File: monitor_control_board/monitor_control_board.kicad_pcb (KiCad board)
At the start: 2 copper layers, 50 x 65.1 mm, 10 parts, among them J1 Conn_01x08_Male, J2 Conn_01x08_Male, J3 Conn_01x08_Male, SW1 SW_Push, SW2 SW_Push, SW3 SW_Push, SW4 SW_Push, SW5 SW_Push, SW6 SW_Push

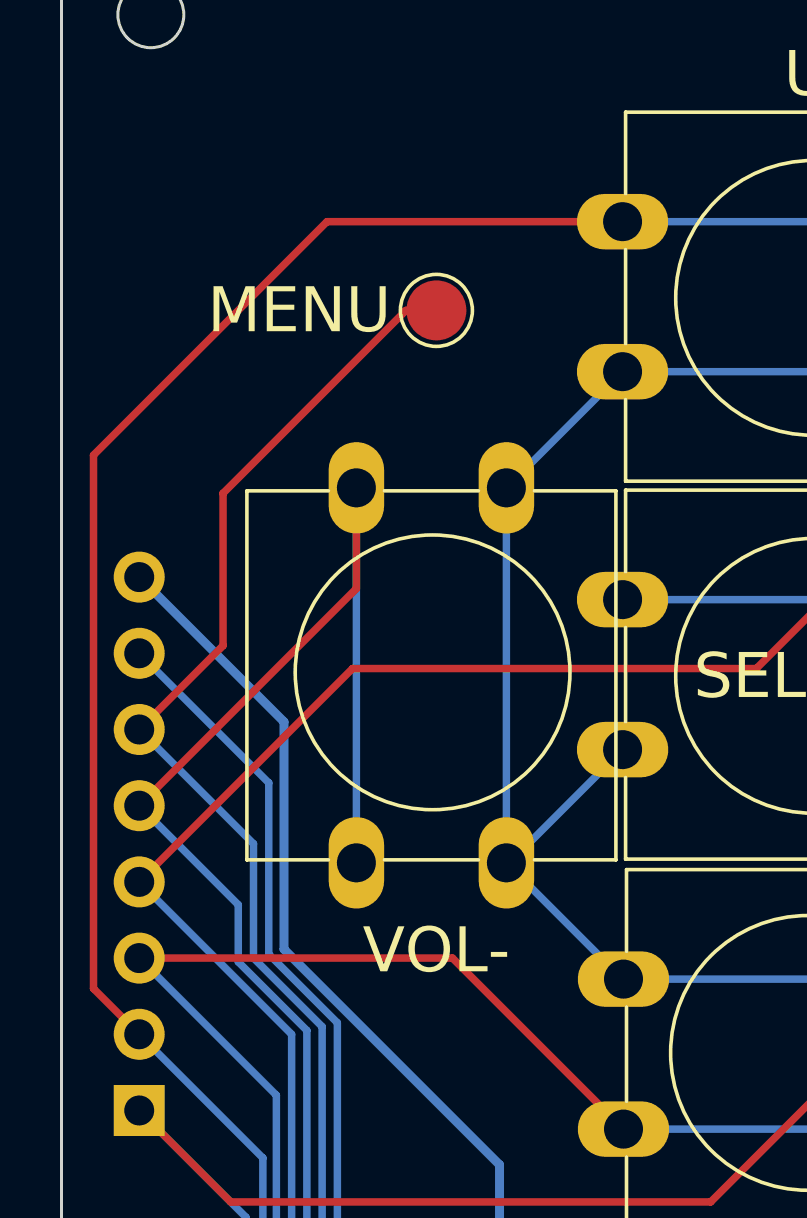
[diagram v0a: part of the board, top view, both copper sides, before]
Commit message: monitor control board에 GND TP 추가
Signed-off-by: Ju, Gyeong-min <jcmh74@gmail.com>
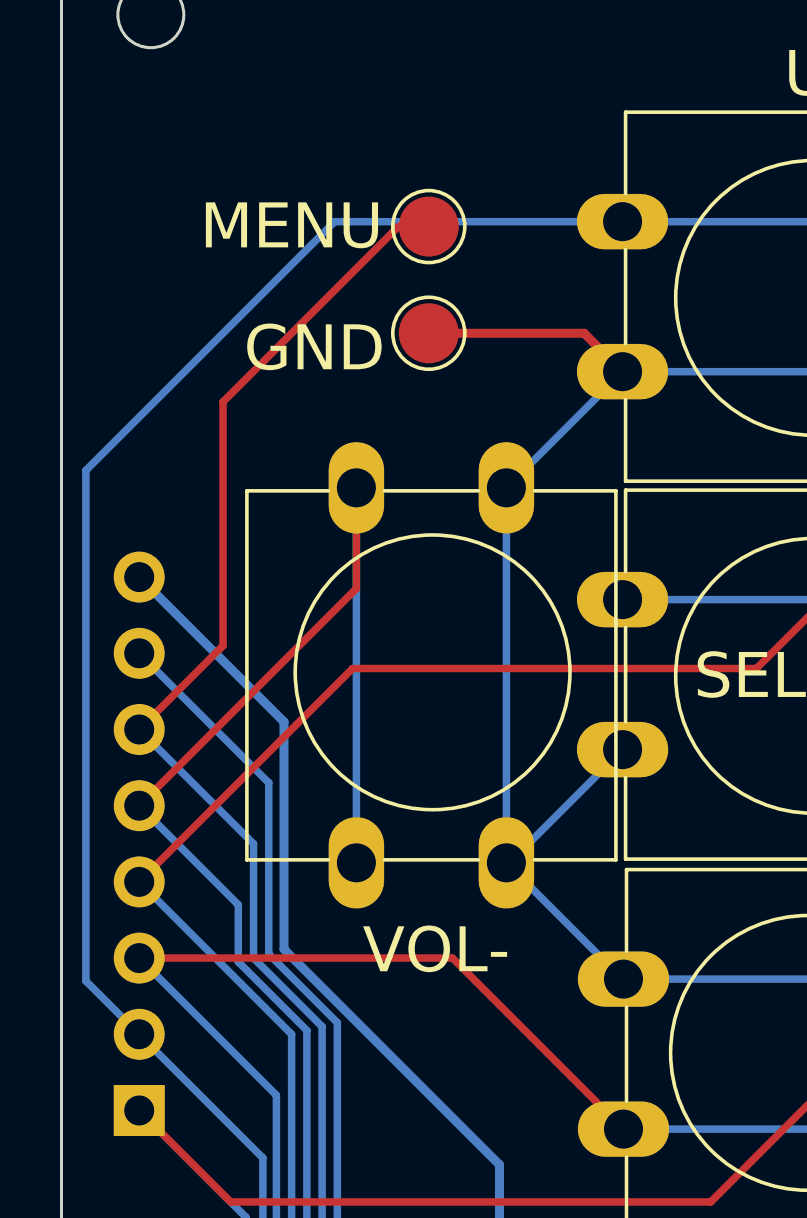
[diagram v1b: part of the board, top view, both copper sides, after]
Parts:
- added TP2: TestPoint, TestPoint:TestPoint_Pad_D2.0mm, F.Cu at (141.0, 71.4)
- moved TP1 2.81 mm to (141.0, 67.8)
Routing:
- net GND: track 198.2 -> 205.2 mm
- net /MENU: track 67.3 -> 70.0 mm
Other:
- board text added: "GND"
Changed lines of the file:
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@@
   )
   (footprint "TestPoint:TestPoint_Pad_D2.0mm" (layer "F.Cu")
-    (at 141.224 70.612)
+    (at 140.97 67.818)
     (descr "SMD pad as test Point, diameter 2.0mm")
     (tags "test point SMD pad")
@@
     )
   )
+  (footprint "TestPoint:TestPoint_Pad_D2.0mm" (layer "F.Cu")
+    (at 140.97 71.374)
+    (descr "SMD pad as test Point, diameter 2.0mm")
+    (tags "test point SMD pad")
+    (property "Sheetfile" "monitor_control_board.kicad_sch")
+    (property "Sheetname" "")
+    (attr exclude_from_pos_files)
+    (fp_text reference "TP2" (at 0 -1.998) (layer "F.SilkS") hide
+      (effects (font (size 1 1) (thickness 0.15)))
+    )
+    (fp_text value "TestPoint" (at 0 2.05) (layer "F.Fab")
+      (effects (font (size 1 1) (thickness 0.15)))
+    )
+    (fp_text user "${REFERENCE}" (at 0 -2) (layer "F.Fab")
+      (effects (font (size 1 1) (thickness 0.15)))
+    )
+    (fp_circle (center 0 0) (end 0 1.2) (layer "F.SilkS") (width 0.12) (fill none))
+    (fp_circle (center 0 0) (end 1.5 0) (layer "F.CrtYd") (width 0.05) (fill none))
+    (pad "1" smd circle (at 0 0) (size 2 2) (layers "F.Cu" "F.Mask")
+      (net 7 "GND") (pinfunction "1") (pintype "passive"))
+  )
   (footprint "Button_Switch_THT:SW_PUSH-12mm" (layer "F.Cu")
     (at 159.9608 97.9024 180)
@@
     (effects (font (size 1.5 1.5) (thickness 0.3)))
   )
-  (gr_text "MENU" (at 136.652 70.612) (layer "F.SilkS")
+  (gr_text "MENU" (at 136.398 67.818) (layer "F.SilkS")
     (effects (font (size 1.5 1.5) (thickness 0.3)))
   )
@@
     (effects (font (size 1.5 1.5) (thickness 0.3)))
   )
+  (gr_text "GND" (at 137.16 71.882) (layer "F.SilkS")
+    (effects (font (size 1.5 1.5) (thickness 0.3)))
+  )
   (gr_text "VOL+" (at 166.37 91.948) (layer "F.SilkS")
     (effects (font (size 1.5 1.5) (thickness 0.3)))
@@
   (segment (start 162.052 117.602) (end 159.766 119.888) (width 0.3) (layer "B.Cu") (net 1))
   (segment (start 134.874 100.838) (end 131.318 97.282) (width 0.25) (layer "B.Cu") (net 1))
-  (segment (start 131.318 94.742) (end 129.794 93.218) (width 0.25) (layer "F.Cu") (net 2))
-  (segment (start 129.794 93.218) (end 129.794 75.438) (width 0.25) (layer "F.Cu") (net 2))
-  (segment (start 129.794 75.438) (end 137.5772 67.6548) (width 0.25) (layer "F.Cu") (net 2))
-  (segment (start 137.5772 67.6548) (end 147.43 67.6548) (width 0.25) (layer "F.Cu") (net 2))
   (segment (start 144.758 116.056) (end 144.758 117.326) (width 0.25) (layer "B.Cu") (net 2))
   (segment (start 135.44 114.358) (end 135.44 98.864) (width 0.25) (layer "B.Cu") (net 2))
@@
   (segment (start 135.44 98.864) (end 131.318 94.742) (width 0.25) (layer "B.Cu") (net 2))
   (segment (start 146.812 119.38) (end 157.988 119.38) (width 0.25) (layer "B.Cu") (net 2))
+  (segment (start 129.54 92.964) (end 129.54 75.946) (width 0.25) (layer "B.Cu") (net 2))
   (segment (start 136.729 115.647) (end 135.44 114.358) (width 0.25) (layer "B.Cu") (net 2))
   (segment (start 144.349 115.647) (end 144.758 116.056) (width 0.25) (layer "B.Cu") (net 2))
@@
   (segment (start 143.328 115.647) (end 144.349 115.647) (width 0.25) (layer "B.Cu") (net 2))
   (segment (start 157.988 119.38) (end 160.052 117.316) (width 0.25) (layer "B.Cu") (net 2))
+  (segment (start 131.318 94.742) (end 129.54 92.964) (width 0.25) (layer "B.Cu") (net 2))
   (segment (start 143.328 115.647) (end 136.729 115.647) (width 0.25) (layer "B.Cu") (net 2))
+  (segment (start 137.8312 67.6548) (end 147.43 67.6548) (width 0.25) (layer "B.Cu") (net 2))
+  (segment (start 129.54 75.946) (end 137.8312 67.6548) (width 0.25) (layer "B.Cu") (net 2))
   (segment (start 144.758 117.326) (end 146.812 119.38) (width 0.25) (layer "B.Cu") (net 2))
   (segment (start 166.5416 78.74) (end 168.8192 76.4624) (width 0.25) (layer "F.Cu") (net 3))
@@
   (segment (start 148.052 115.346) (end 150.876 112.522) (width 0.3) (layer "F.Cu") (net 7))
   (segment (start 150.876 112.522) (end 167.386 112.522) (width 0.3) (layer "F.Cu") (net 7))
+  (segment (start 140.97 71.374) (end 146.1492 71.374) (width 0.3) (layer "F.Cu") (net 7))
+  (segment (start 146.1492 71.374) (end 147.43 72.6548) (width 0.3) (layer "F.Cu") (net 7))
   (segment (start 147.43 72.6548) (end 147.4292 72.6548) (width 0.25) (layer "B.Cu") (net 7))
   (segment (start 143.328 108.147) (end 169.5914 108.147) (width 0.25) (layer "B.Cu") (net 7))
@@
   (segment (start 169.5914 108.147) (end 170.9208 109.4764) (width 0.25) (layer "B.Cu") (net 7))
   (segment (start 147.4608 92.9024) (end 147.4324 92.9024) (width 0.25) (layer "B.Cu") (net 7))
-  (segment (start 140.208 70.612) (end 141.224 70.612) (width 0.25) (layer "F.Cu") (net 8))
-  (segment (start 134.112 76.708) (end 140.208 70.612) (width 0.25) (layer "F.Cu") (net 8))
+  (segment (start 139.954 67.818) (end 140.97 67.818) (width 0.25) (layer "F.Cu") (net 8))
+  (segment (start 134.112 73.66) (end 139.954 67.818) (width 0.25) (layer "F.Cu") (net 8))
   (segment (start 131.318 84.582) (end 134.112 81.788) (width 0.25) (layer "F.Cu") (net 8))
-  (segment (start 134.112 81.788) (end 134.112 76.708) (width 0.25) (layer "F.Cu") (net 8))
+  (segment (start 134.112 81.788) (end 134.112 73.66) (width 0.25) (layer "F.Cu") (net 8))
   (segment (start 137.414 109.474) (end 137.414 94.485208) (width 0.25) (layer "B.Cu") (net 8))
   (segment (start 138.587 110.647) (end 137.414 109.474) (width 0.25) (layer "B.Cu") (net 8))

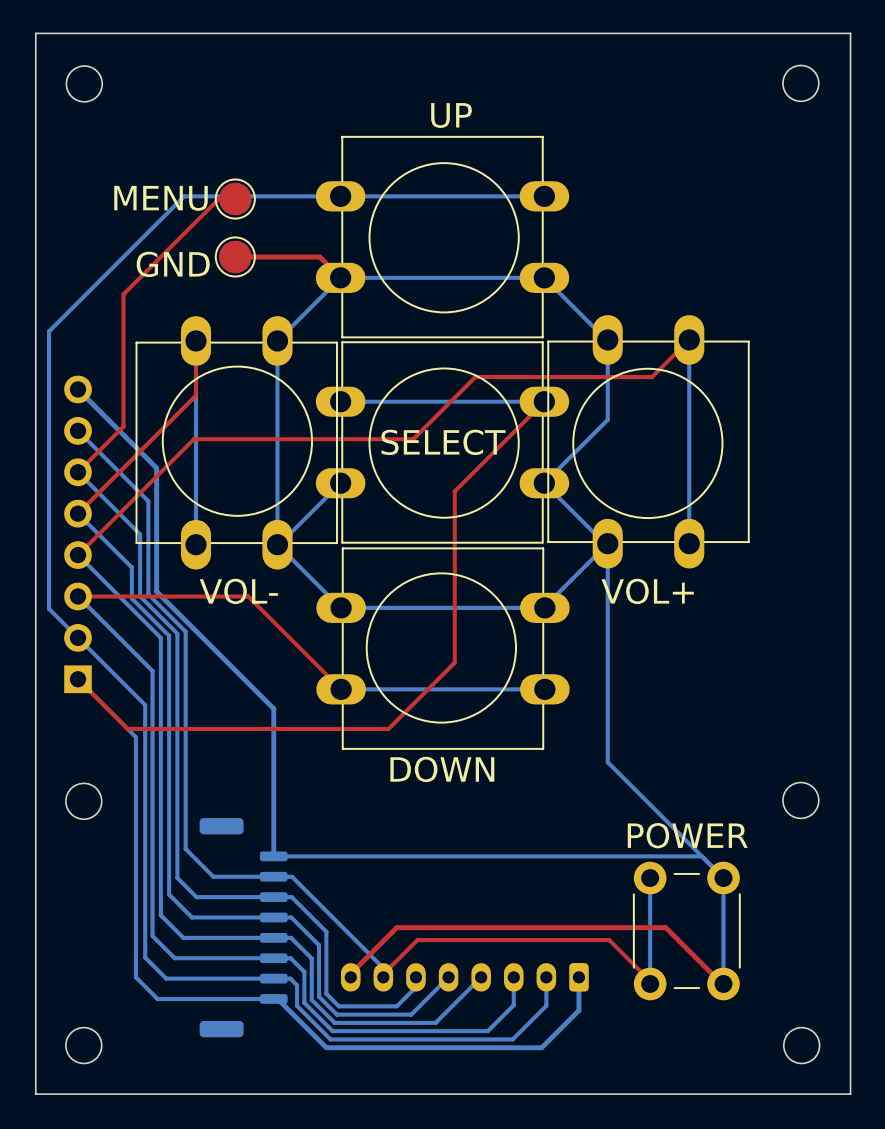
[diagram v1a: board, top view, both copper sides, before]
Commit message: monitor_control_board rev2 업데이트
Signed-off-by: Ju, Gyeong-min <jcmh74@gmail.com>
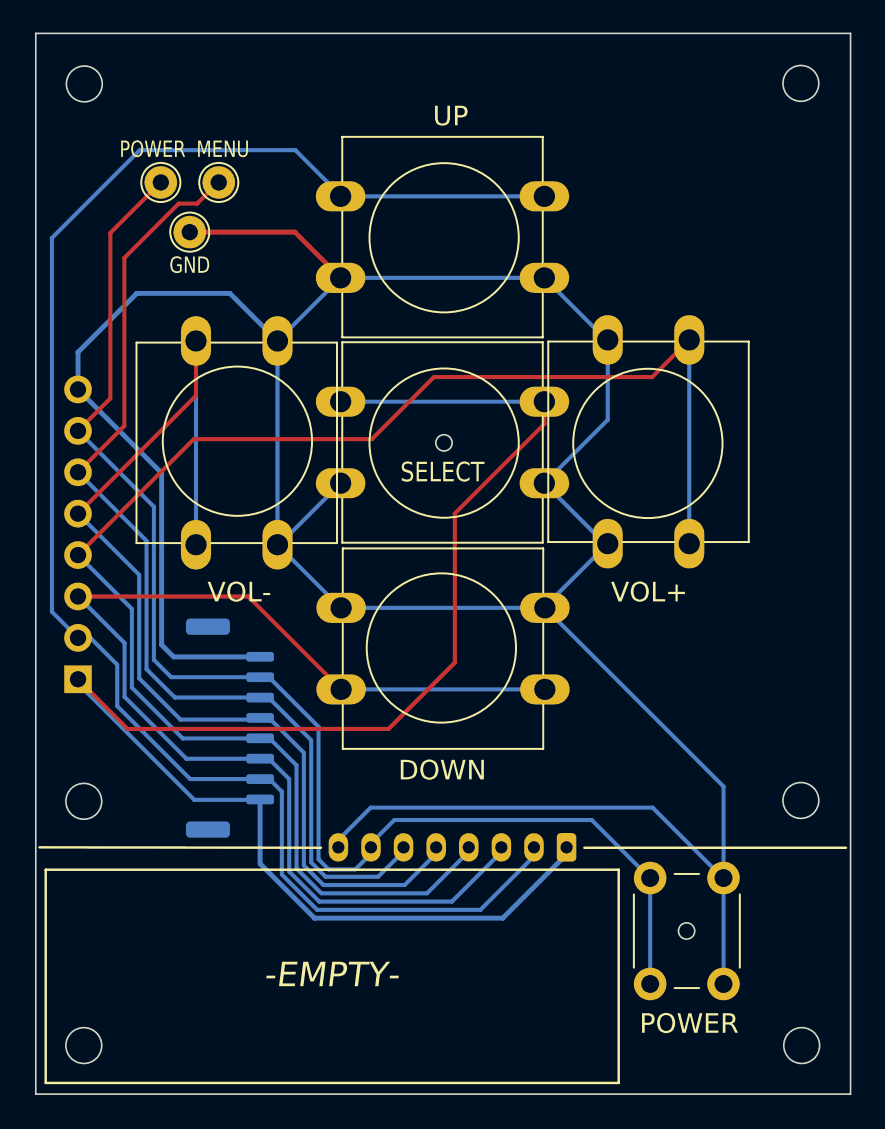
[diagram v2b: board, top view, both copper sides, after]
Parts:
- added TP3: TestPoint, TestPoint:TestPoint_THTPad_D2.0mm_Drill1.0mm, F.Cu at (136.4, 66.8)
- TP1, TP2: footprint TestPoint:TestPoint_Pad_D2.0mm -> TestPoint:TestPoint_THTPad_D2.0mm_Drill1.0mm
- moved J1 12.3 mm to (140.6, 100.3)
- moved J3 8.01 mm to (161.3, 107.6)
- moved TP2 3.18 mm to (138.2, 69.8)
- moved TP1 1.44 mm to (140.0, 66.8)
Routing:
- net GND: track 205.2 -> 186.9 mm
- net /POWER: track 69.3 -> 83.5 mm
- net /SELECT: track 108.6 -> 97.4 mm
- net /DOWN: track 81.8 -> 71.5 mm
- net /VOL_P: track 104.7 -> 95.9 mm
- net /VOL_M: track 74.8 -> 66.5 mm
- net /MENU: track 70.0 -> 62.2 mm
- net /UP: track 104.7 -> 100.1 mm
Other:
- outline, holes or cut-outs redrawn
- board text added: "-EMPTY-"
- board text added: "Monitor Control Board Rev.2"
- board text removed: "Monitor Control Board Rev.1"

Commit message: monitor_control_board 레이아웃 정밀성 향상
Signed-off-by: Ju, Gyeong-min <jcmh74@gmail.com>
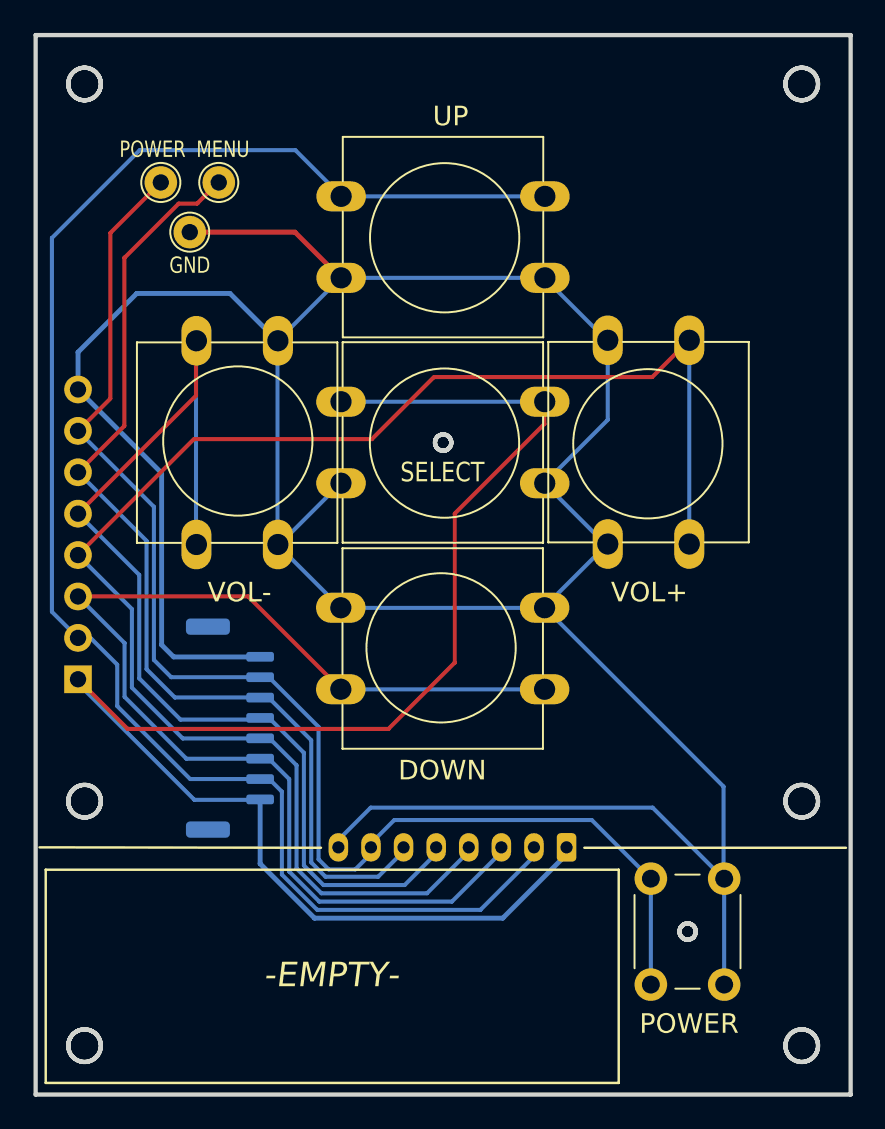
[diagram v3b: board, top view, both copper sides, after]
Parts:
- moved SW6 0.06 mm to (166.5, 116.0)
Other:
- board size 50 x 65.1 mm -> 50 x 65 mm

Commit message: rasp_power_module smt 관련 작업 추가 및 monitor_control_board 개선
Signed-off-by: Ju, Gyeong-min <jcmh74@gmail.com>
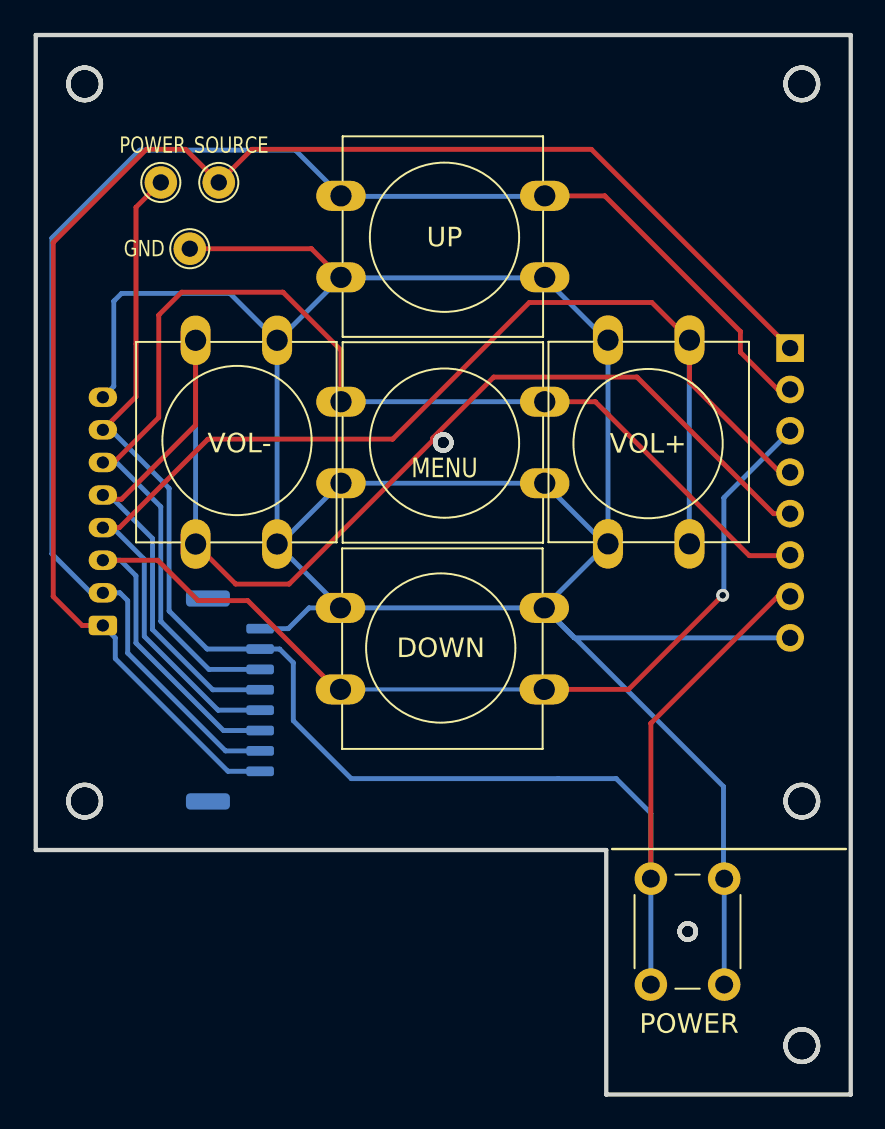
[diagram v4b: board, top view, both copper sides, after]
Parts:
- moved J2 48.2 mm to (175.0, 77.0), turned to 180 degrees
- moved J3 31.5 mm to (132.8, 94.0), turned to 90 degrees
- moved J1 1.73 mm to (140.6, 98.6)
- moved TP2 1.02 mm to (138.2, 70.9)
- moved SW1 0.06 mm to (138.5, 89.0)
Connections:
- J1 pad 1: /SELECT -> /SOURCE
- J2 pad 1: /SELECT -> /SOURCE
- J3 pad 1: /SELECT -> /SOURCE
- SW3 pad 1: /SELECT -> /MENU
- TP1 pad 1: /MENU -> /SOURCE
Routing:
- net /SELECT: track 97.4 -> 0.00 mm
- net /SOURCE: track 0.00 -> 93.9 mm
- net /VOL_M: track 66.5 -> 88.7 mm
- net /MENU: track 62.2 -> 77.8 mm
- net GND: track 186.9 -> 171.9 mm
- net /POWER: track 83.5 -> 98.3 mm
- net /VOL_P: track 95.9 -> 83.2 mm
- net /UP: track 100.1 -> 93.4 mm
- net /DOWN: track 71.5 -> 71.9 mm, vias 0 -> 1
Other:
- outline, holes or cut-outs redrawn
- board text added: "Conn_01x08_Male"
- board text added: "J3"
- board text added: "JLCJLCJLCJLC"
- board text added: "Monitor Control Board Rev.3"
- board text added: "SOURCE"
- board text added: "SRC"
- board text removed: "-EMPTY-"
- board text removed: "Monitor Control Board Rev.2"
- board text removed: "SEL"
- board text removed: "SELECT"
